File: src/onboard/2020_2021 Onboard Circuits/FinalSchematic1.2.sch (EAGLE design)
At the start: 80 parts, among them IC1 MIC2937A-5.0BT, IC3 A5975D

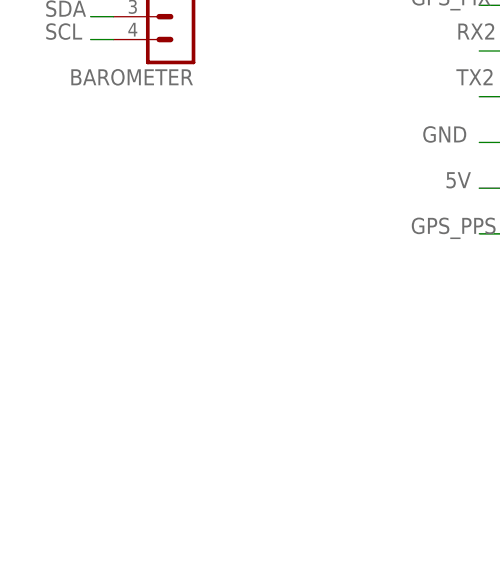
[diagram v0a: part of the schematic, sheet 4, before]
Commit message: Added BMP280 I2C Part
Added to SCH sheet 4
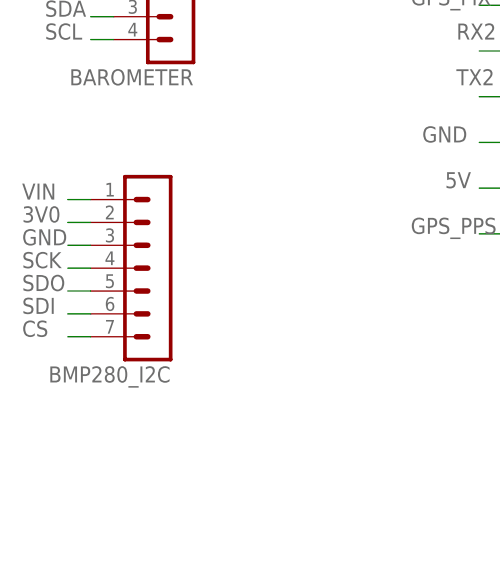
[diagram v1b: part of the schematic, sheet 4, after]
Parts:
- added BMP280_I2C: (no value), con-lstb:MA07-1
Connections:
- new net 3V0: BMP280_I2C.2
- new net CS: BMP280_I2C.7
- new net SCK: BMP280_I2C.4
- new net SDI: BMP280_I2C.6
- new net SDO: BMP280_I2C.5
- new net VIN: BMP280_I2C.1
- net GND: now also BMP280_I2C.3

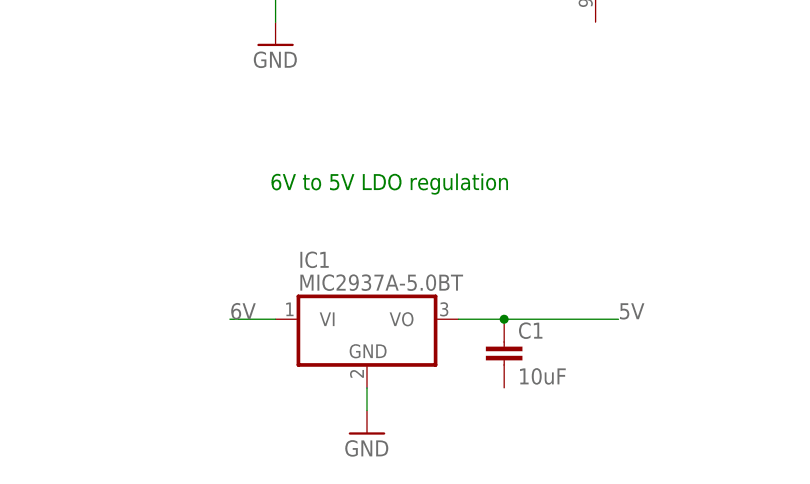
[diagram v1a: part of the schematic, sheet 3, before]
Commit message: Switched 6v LDO to MIC29310-5.0BT
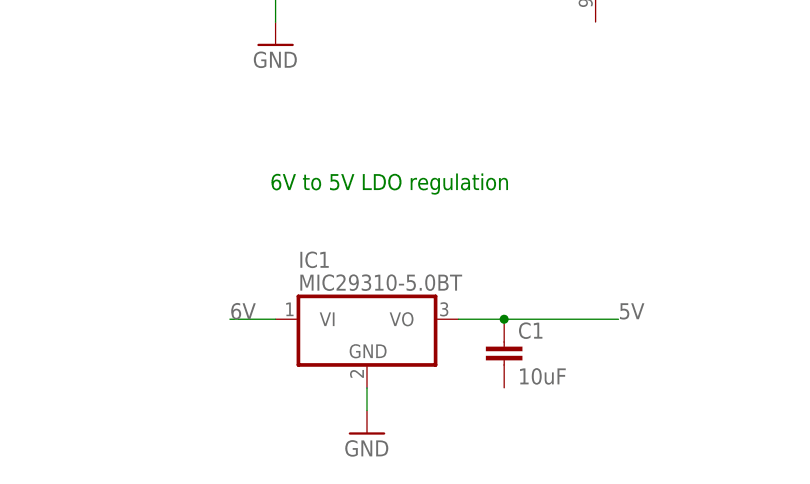
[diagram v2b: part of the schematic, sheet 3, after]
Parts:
- IC1: value MIC2937A-5.0BT -> MIC29310-5.0BT
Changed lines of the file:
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@@
 <grid distance="0.1" unitdist="inch" unit="inch" style="lines" multiple="1" display="no" altdistance="0.01" altunitdist="inch" altunit="inch"/>
 <layers>
-<layer number="1" name="Top" color="4" fill="1" visible="yes" active="no"/>
-<layer number="2" name="Route2" color="16" fill="1" visible="yes" active="no"/>
-<layer number="3" name="Route3" color="17" fill="1" visible="yes" active="no"/>
-<layer number="4" name="Route4" color="18" fill="1" visible="yes" active="no"/>
-<layer number="5" name="Route5" color="19" fill="1" visible="yes" active="no"/>
-<layer number="6" name="Route6" color="25" fill="1" visible="yes" active="no"/>
-<layer number="7" name="Route7" color="26" fill="1" visible="yes" active="no"/>
-<layer number="8" name="Route8" color="27" fill="1" visible="yes" active="no"/>
-<layer number="9" name="Route9" color="28" fill="1" visible="yes" active="no"/>
-<layer number="10" name="Route10" color="29" fill="1" visible="yes" active="no"/>
-<layer number="11" name="Route11" color="30" fill="1" visible="yes" active="no"/>
-<layer number="12" name="Route12" color="20" fill="1" visible="yes" active="no"/>
-<layer number="13" name="Route13" color="21" fill="1" visible="yes" active="no"/>
-<layer number="14" name="Route14" color="22" fill="1" visible="yes" active="no"/>
-<layer number="15" name="Route15" color="23" fill="1" visible="yes" active="no"/>
-<layer number="16" name="Bottom" color="1" fill="1" visible="yes" active="no"/>
-<layer number="17" name="Pads" color="2" fill="1" visible="yes" active="no"/>
-<layer number="18" name="Vias" color="2" fill="1" visible="yes" active="no"/>
-<layer number="19" name="Unrouted" color="6" fill="1" visible="yes" active="no"/>
-<layer number="20" name="Dimension" color="24" fill="1" visible="yes" active="no"/>
-<layer number="21" name="tPlace" color="7" fill="1" visible="yes" active="no"/>
-<layer number="22" name="bPlace" color="7" fill="1" visible="yes" active="no"/>
-<layer number="23" name="tOrigins" color="15" fill="1" visible="yes" active="no"/>
-<layer number="24" name="bOrigins" color="15" fill="1" visible="yes" active="no"/>
-<layer number="25" name="tNames" color="7" fill="1" visible="yes" active="no"/>
-<layer number="26" name="bNames" color="7" fill="1" visible="yes" active="no"/>
-<layer number="27" name="tValues" color="7" fill="1" visible="yes" active="no"/>
-<layer number="28" name="bValues" color="7" fill="1" visible="yes" active="no"/>
+<layer number="1" name="Top" color="4" fill="1" visible="no" active="no"/>
+<layer number="2" name="Route2" color="16" fill="1" visible="no" active="no"/>
+<layer number="3" name="Route3" color="17" fill="1" visible="no" active="no"/>
+<layer number="4" name="Route4" color="18" fill="1" visible="no" active="no"/>
+<layer number="5" name="Route5" color="19" fill="1" visible="no" active="no"/>
+<layer number="6" name="Route6" color="25" fill="1" visible="no" active="no"/>
+<layer number="7" name="Route7" color="26" fill="1" visible="no" active="no"/>
+<layer number="8" name="Route8" color="27" fill="1" visible="no" active="no"/>
+<layer number="9" name="Route9" color="28" fill="1" visible="no" active="no"/>
+<layer number="10" name="Route10" color="29" fill="1" visible="no" active="no"/>
+<layer number="11" name="Route11" color="30" fill="1" visible="no" active="no"/>
+<layer number="12" name="Route12" color="20" fill="1" visible="no" active="no"/>
+<layer number="13" name="Route13" color="21" fill="1" visible="no" active="no"/>
+<layer number="14" name="Route14" color="22" fill="1" visible="no" active="no"/>
+<layer number="15" name="Route15" color="23" fill="1" visible="no" active="no"/>
+<layer number="16" name="Bottom" color="1" fill="1" visible="no" active="no"/>
+<layer number="17" name="Pads" color="2" fill="1" visible="no" active="no"/>
+<layer number="18" name="Vias" color="2" fill="1" visible="no" active="no"/>
+<layer number="19" name="Unrouted" color="6" fill="1" visible="no" active="no"/>
+<layer number="20" name="Dimension" color="24" fill="1" visible="no" active="no"/>
+<layer number="21" name="tPlace" color="7" fill="1" visible="no" active="no"/>
+<layer number="22" name="bPlace" color="7" fill="1" visible="no" active="no"/>
+<layer number="23" name="tOrigins" color="15" fill="1" visible="no" active="no"/>
+<layer number="24" name="bOrigins" color="15" fill="1" visible="no" active="no"/>
+<layer number="25" name="tNames" color="7" fill="1" visible="no" active="no"/>
+<layer number="26" name="bNames" color="7" fill="1" visible="no" active="no"/>
+<layer number="27" name="tValues" color="7" fill="1" visible="no" active="no"/>
+<layer number="28" name="bValues" color="7" fill="1" visible="no" active="no"/>
 <layer number="29" name="tStop" color="7" fill="3" visible="no" active="no"/>
 <layer number="30" name="bStop" color="7" fill="6" visible="no" active="no"/>
@@
 <layer number="35" name="tGlue" color="7" fill="4" visible="no" active="no"/>
 <layer number="36" name="bGlue" color="7" fill="5" visible="no" active="no"/>
-<layer number="37" name="tTest" color="7" fill="1" visible="yes" active="no"/>
-<layer number="38" name="bTest" color="7" fill="1" visible="yes" active="no"/>
+<layer number="37" name="tTest" color="7" fill="1" visible="no" active="no"/>
+<layer number="38" name="bTest" color="7" fill="1" visible="no" active="no"/>
 <layer number="39" name="tKeepout" color="4" fill="11" visible="no" active="no"/>
 <layer number="40" name="bKeepout" color="1" fill="11" visible="no" active="no"/>
@@
 <layer number="44" name="Drills" color="7" fill="1" visible="no" active="no"/>
 <layer number="45" name="Holes" color="7" fill="1" visible="no" active="no"/>
-<layer number="46" name="Milling" color="3" fill="1" visible="yes" active="no"/>
-<layer number="47" name="Measures" color="7" fill="1" visible="yes" active="no"/>
-<layer number="48" name="Document" color="7" fill="1" visible="yes" active="no"/>
-<layer number="49" name="Reference" color="7" fill="1" visible="yes" active="no"/>
-<layer number="50" name="dxf" color="7" fill="1" visible="yes" active="no"/>
-<layer number="51" name="tDocu" color="7" fill="1" visible="yes" active="no"/>
-<layer number="52" name="bDocu" color="7" fill="1" visible="yes" active="no"/>
-<layer number="53" name="tGND_GNDA" color="7" fill="9" visible="yes" active="no"/>
-<layer number="54" name="bGND_GNDA" color="1" fill="9" visible="yes" active="no"/>
-<layer number="56" name="wert" color="7" fill="1" visible="yes" active="no"/>
-<layer number="57" name="tCAD" color="7" fill="1" visible="yes" active="no"/>
-<layer number="59" name="tCarbon" color="7" fill="1" visible="yes" active="no"/>
-<layer number="60" name="bCarbon" color="7" fill="1" visible="yes" active="no"/>
+<layer number="46" name="Milling" color="3" fill="1" visible="no" active="no"/>
+<layer number="47" name="Measures" color="7" fill="1" visible="no" active="no"/>
+<layer number="48" name="Document" color="7" fill="1" visible="no" active="no"/>
+<layer number="49" name="Reference" color="7" fill="1" visible="no" active="no"/>
+<layer number="50" name="dxf" color="7" fill="1" visible="no" active="no"/>
+<layer number="51" name="tDocu" color="7" fill="1" visible="no" active="no"/>
+<layer number="52" name="bDocu" color="7" fill="1" visible="no" active="no"/>
+<layer number="53" name="tGND_GNDA" color="7" fill="9" visible="no" active="no"/>
+<layer number="54" name="bGND_GNDA" color="1" fill="9" visible="no" active="no"/>
+<layer number="56" name="wert" color="7" fill="1" visible="no" active="no"/>
+<layer number="57" name="tCAD" color="7" fill="1" visible="no" active="no"/>
+<layer number="59" name="tCarbon" color="7" fill="1" visible="no" active="no"/>
+<layer number="60" name="bCarbon" color="7" fill="1" visible="no" active="no"/>
 <layer number="88" name="SimResults" color="9" fill="1" visible="yes" active="yes"/>
 <layer number="89" name="SimProbes" color="9" fill="1" visible="yes" active="yes"/>
@@
 <part name="GND7" library="supply1" library_urn="urn:adsk.eagle:library:371" deviceset="GND" device=""/>
 <part name="5V_PWR" library="pinhead" library_urn="urn:adsk.eagle:library:325" deviceset="PINHD-1X3" device="" package3d_urn="urn:adsk.eagle:package:22458/2"/>
-<part name="IC1" library="linear" library_urn="urn:adsk.eagle:library:262" deviceset="78*" device="TV" package3d_urn="urn:adsk.eagle:package:16417/2" technology="6" value="MIC2937A-5.0BT"/>
+<part name="IC1" library="linear" library_urn="urn:adsk.eagle:library:262" deviceset="78*" device="TV" package3d_urn="urn:adsk.eagle:package:16417/2" technology="6" value="MIC29310-5.0BT"/>
 <part name="GND8" library="supply1" library_urn="urn:adsk.eagle:library:371" deviceset="GND" device=""/>
 <part name="C1" library="capacitor-wima" library_urn="urn:adsk.eagle:library:116" deviceset="C" device="2,5-3" package3d_urn="urn:adsk.eagle:package:5436/1" value="10uF"/>
